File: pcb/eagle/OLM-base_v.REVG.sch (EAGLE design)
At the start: 40 parts, among them IC1 ATMEGA, IC2 MCP1702-33, IC3 ENC28J60SP, IC4 DS1307, J1 POWER_JACKPTH, J2 MAGJACK, U1 USD-SOCKETMICRO-SD-SOCKET-TAO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, X1 16 MHz, X2 25MHz, X3 32.657k

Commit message: made changes
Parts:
- removed JP1: BATT, SparkFun:M02LOCK_LONGPADS
- removed JP2: (no value), SparkFun-Connectors:M08LOCK
- added CN1: (no value), adafruit:JST_2PIN-THM-RA
- added JP4: M10LOCK, SparkFun-Connectors:M10LOCK
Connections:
- net A4/SDA: now also JP4.10; no longer JP2.8
- net A5/SCL: now also JP4.9; no longer JP2.7
- net D2: now also JP4.3; no longer JP2.4
- net D3/PWM: now also JP4.2; no longer JP2.3
- net D4: now also JP4.6
- net D6/PWM: now also JP4.5
- net D7: now also JP4.4
- net E-CLK: now also JP4.8; no longer JP2.6
- net E-INT: now also JP4.7; no longer JP2.5
- net GND: now also CN1.1, JP4.1; no longer JP1.2, JP2.1
- net MISO/D12: now also U1.DO
- net MOSI/D11: now also U1.DI
- net SCK/D13: now also U1.SCK
- net VCC: now also JP3.8; no longer JP2.2
- net VIN: now also CN1.2; no longer JP1.1, JP3.8
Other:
- note added: "328p"
- note added: "Breakout"
- note added: "Ethernet"
- note added: "RTC"
- note added: "uSD"
- note removed: "UNO-Compatible"
- moved on the sheet: BAT1, CR, IC4, JP3, RN1-2, RN1-3, RN1-4, RN1-5, U1, X3

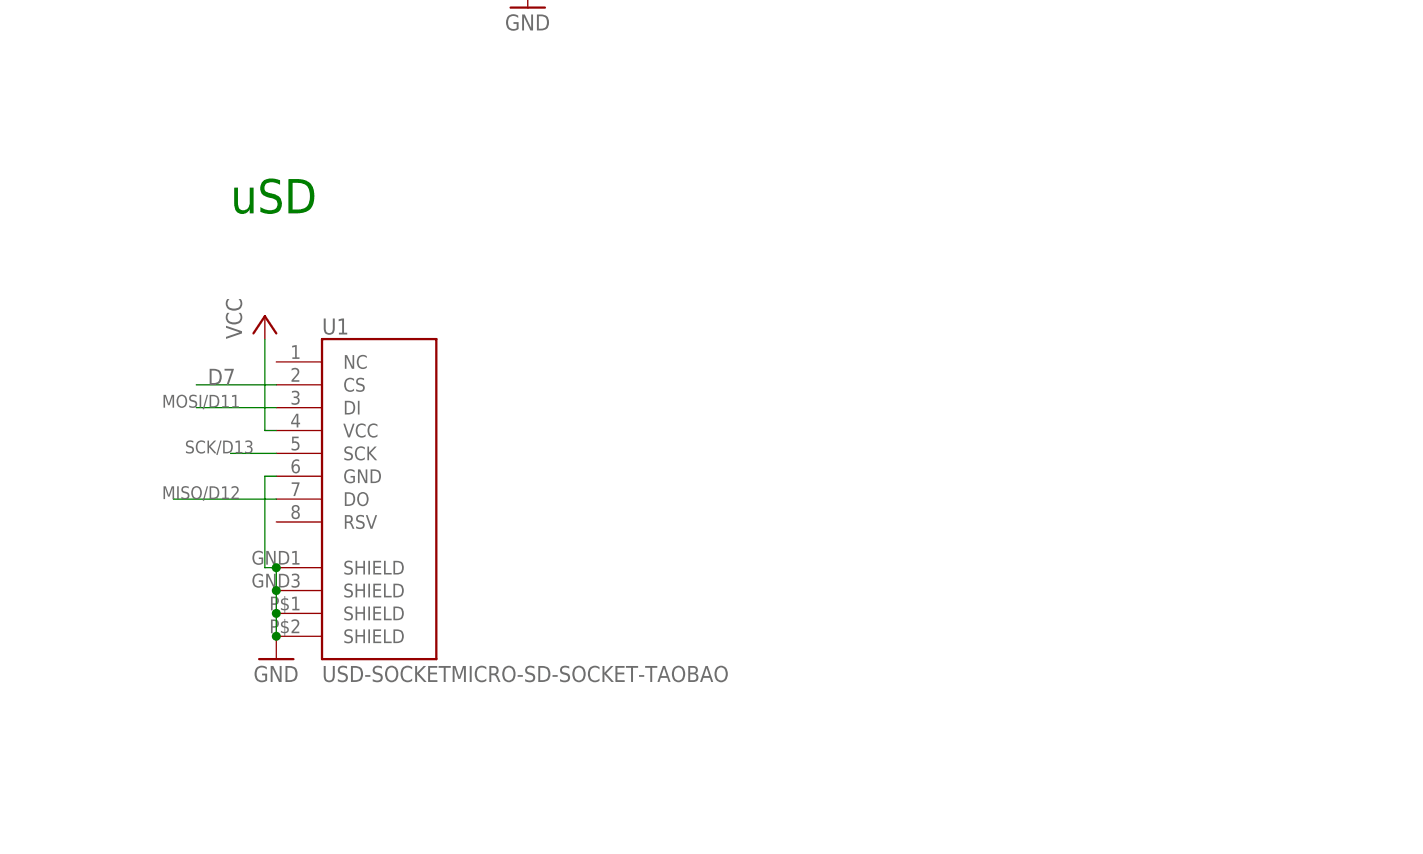
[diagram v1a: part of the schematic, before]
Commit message: rewired OLM-base-REVG
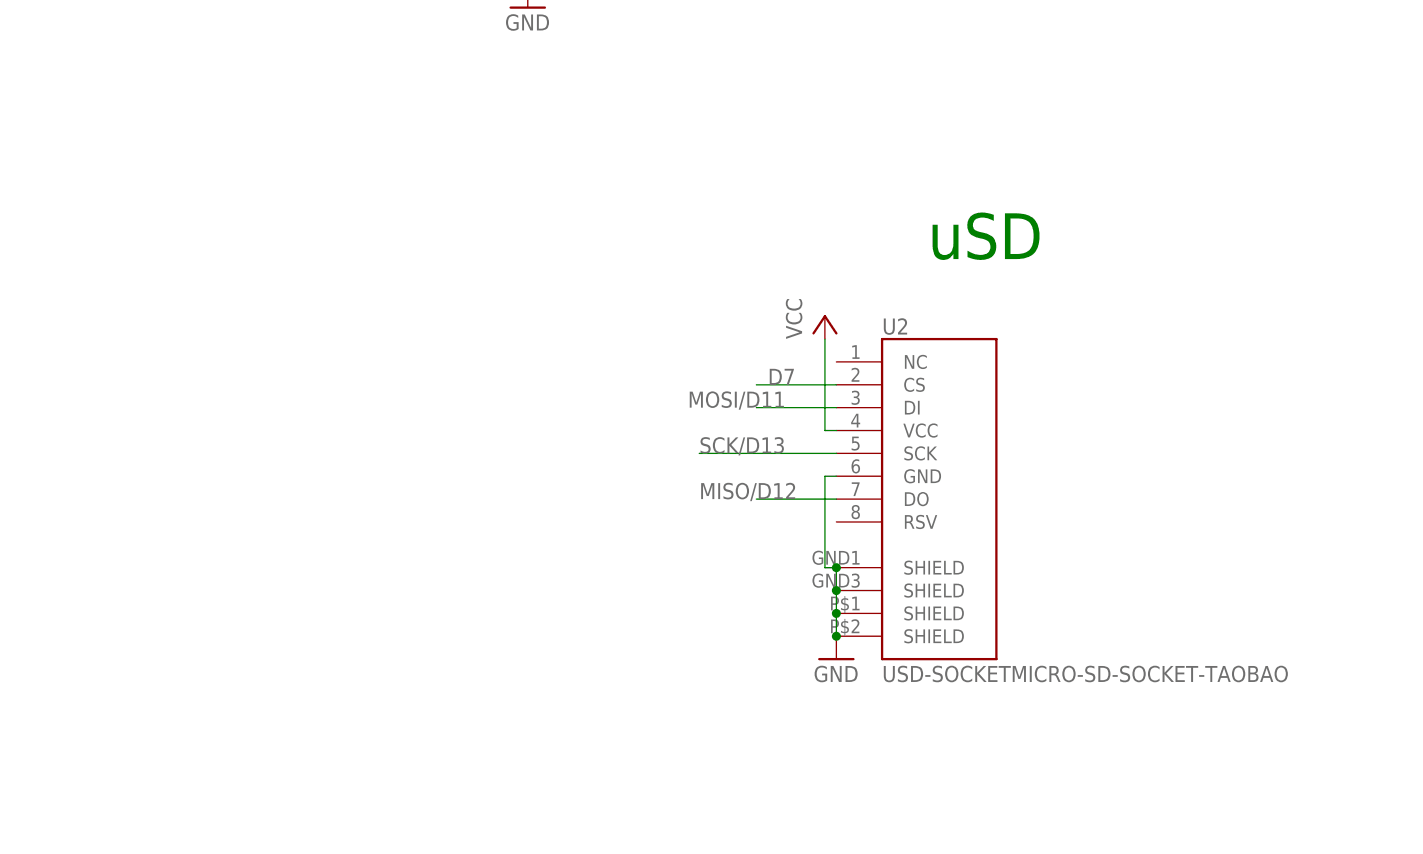
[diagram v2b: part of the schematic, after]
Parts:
- removed U1: USD-SOCKETMICRO-SD-SOCKET-TAOBAO, SparkFunNew:USD-SOCKETMICRO-SD-SOCKET-TAOBAO
- added U2: USD-SOCKETMICRO-SD-SOCKET-TAOBAO, SparkFunNew:USD-SOCKETMICRO-SD-SOCKET-TAOBAO
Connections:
- net D7: now also U2.CS; no longer U1.CS
- net GND: now also U2.GND, U2.SHIELD@1, U2.SHIELD@2, U2.SHIELD@3, U2.SHIELD@4; no longer U1.GND, U1.SHIELD@1, U1.SHIELD@2, U1.SHIELD@3, U1.SHIELD@4
- net MISO/D12: now also U2.DO; no longer U1.DO
- net MOSI/D11: now also U2.DI; no longer U1.DI
- net SCK/D13: now also U2.SCK; no longer U1.SCK
- net VCC: now also U2.VCC; no longer U1.VCC
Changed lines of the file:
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@@
 <part name="RN1" library="resistor-net" deviceset="RNX7" device=""/>
 <part name="JP3" library="SparkFun-Connectors" deviceset="M08" device="LOCK"/>
-<part name="U1" library="SparkFunNew" deviceset="USD-SOCKET" device="MICRO-SD-SOCKET-TAOBAO" value="USD-SOCKETMICRO-SD-SOCKET-TAOBAO"/>
-<part name="GND5" library="SparkFun" deviceset="GND" device=""/>
-<part name="+3V3" library="supply1" deviceset="VCC" device=""/>
 <part name="JP4" library="SparkFun-Connectors" deviceset="M10" device="LOCK"/>
 <part name="CN1" library="adafruit" deviceset="JST_2PIN" device="-THM-RA"/>
+<part name="U2" library="SparkFunNew" deviceset="USD-SOCKET" device="MICRO-SD-SOCKET-TAOBAO" value="USD-SOCKETMICRO-SD-SOCKET-TAOBAO"/>
+<part name="GND3" library="SparkFun" deviceset="GND" device=""/>
+<part name="+3V1" library="supply1" deviceset="VCC" device=""/>
 </parts>
 <sheets>
@@
 <text x="127" y="76.2" size="3.81" layer="91">Ethernet</text>
 <text x="0" y="-124.46" size="3.81" layer="91">RTC</text>
-<text x="91.44" y="-93.98" size="3.81" layer="91">uSD</text>
+<text x="168.91" y="-99.06" size="5.08" layer="91">uSD</text>
 </plain>
 <instances>
@@
 <instance part="RN1" gate="-5" x="8.89" y="-157.48" rot="MR90"/>
 <instance part="JP3" gate="G$1" x="35.56" y="-25.4"/>
-<instance part="U1" gate="G$1" x="104.14" y="-123.19"/>
-<instance part="GND5" gate="1" x="96.52" y="-143.51"/>
-<instance part="+3V3" gate="VCC" x="95.25" y="-105.41"/>
 <instance part="JP4" gate="G$1" x="-10.16" y="-17.78"/>
 <instance part="CN1" gate="G$1" x="-43.18" y="-91.44"/>
+<instance part="U2" gate="G$1" x="166.37" y="-123.19"/>
+<instance part="GND3" gate="1" x="158.75" y="-143.51"/>
+<instance part="+3V1" gate="VCC" x="157.48" y="-105.41"/>
 </instances>
 <busses>
@@
 </segment>
 <segment>
-<pinref part="U1" gate="G$1" pin="SHIELD@1"/>
-<pinref part="U1" gate="G$1" pin="SHIELD@2"/>
-<wire x1="96.52" y1="-133.35" x2="96.52" y2="-135.89" width="0.1524" layer="91"/>
-<pinref part="U1" gate="G$1" pin="SHIELD@3"/>
-<wire x1="96.52" y1="-135.89" x2="96.52" y2="-138.43" width="0.1524" layer="91"/>
-<junction x="96.52" y="-135.89"/>
-<pinref part="U1" gate="G$1" pin="SHIELD@4"/>
-<wire x1="96.52" y1="-138.43" x2="96.52" y2="-140.97" width="0.1524" layer="91"/>
-<junction x="96.52" y="-138.43"/>
-<pinref part="GND5" gate="1" pin="GND"/>
-<junction x="96.52" y="-140.97"/>
-<pinref part="U1" gate="G$1" pin="GND"/>
-<wire x1="96.52" y1="-123.19" x2="95.25" y2="-123.19" width="0.1524" layer="91"/>
-<wire x1="95.25" y1="-123.19" x2="95.25" y2="-133.35" width="0.1524" layer="91"/>
-<wire x1="95.25" y1="-133.35" x2="96.52" y2="-133.35" width="0.1524" layer="91"/>
-<junction x="96.52" y="-133.35"/>
-</segment>
-<segment>
 <pinref part="JP4" gate="G$1" pin="1"/>
 <wire x1="0" y1="-35.56" x2="7.62" y2="-35.56" width="0.1524" layer="91"/>
 <label x="7.62" y="-35.56" size="1.778" layer="95"/>
+</segment>
+<segment>
+<pinref part="U2" gate="G$1" pin="SHIELD@1"/>
+<pinref part="U2" gate="G$1" pin="SHIELD@2"/>
+<wire x1="158.75" y1="-133.35" x2="158.75" y2="-135.89" width="0.1524" layer="91"/>
+<pinref part="U2" gate="G$1" pin="SHIELD@3"/>
+<wire x1="158.75" y1="-135.89" x2="158.75" y2="-138.43" width="0.1524" layer="91"/>
+<junction x="158.75" y="-135.89"/>
+<pinref part="U2" gate="G$1" pin="SHIELD@4"/>
+<wire x1="158.75" y1="-138.43" x2="158.75" y2="-140.97" width="0.1524" layer="91"/>
+<junction x="158.75" y="-138.43"/>
+<pinref part="GND3" gate="1" pin="GND"/>
+<junction x="158.75" y="-140.97"/>
+<pinref part="U2" gate="G$1" pin="GND"/>
+<wire x1="158.75" y1="-123.19" x2="157.48" y2="-123.19" width="0.1524" layer="91"/>
+<wire x1="157.48" y1="-123.19" x2="157.48" y2="-133.35" width="0.1524" layer="91"/>
+<wire x1="157.48" y1="-133.35" x2="158.75" y2="-133.35" width="0.1524" layer="91"/>
+<junction x="158.75" y="-133.35"/>
 </segment>
 </net>
@@
 </segment>
 <segment>
-<pinref part="U1" gate="G$1" pin="VCC"/>
-<wire x1="96.52" y1="-118.11" x2="95.25" y2="-118.11" width="0.1524" layer="91"/>
-<wire x1="95.25" y1="-118.11" x2="95.25" y2="-107.95" width="0.1524" layer="91"/>
-<pinref part="+3V3" gate="VCC" pin="VCC"/>
-</segment>
-<segment>
 <pinref part="JP3" gate="G$1" pin="8"/>
 <wire x1="40.64" y1="-15.24" x2="45.72" y2="-15.24" width="0.1524" layer="91"/>
 <label x="45.72" y="-15.24" size="1.778" layer="95"/>
 </segment>
+<segment>
+<pinref part="U2" gate="G$1" pin="VCC"/>
+<wire x1="158.75" y1="-118.11" x2="157.48" y2="-118.11" width="0.1524" layer="91"/>
+<wire x1="157.48" y1="-118.11" x2="157.48" y2="-107.95" width="0.1524" layer="91"/>
+<pinref part="+3V1" gate="VCC" pin="VCC"/>
+</segment>
 </net>
 <net name="A1" class="0">
@@
 </segment>
 <segment>
-<wire x1="91.44" y1="-120.65" x2="96.52" y2="-120.65" width="0.1524" layer="91"/>
-<label x="86.36" y="-120.65" size="1.4224" layer="95"/>
-<pinref part="U1" gate="G$1" pin="SCK"/>
+<pinref part="U2" gate="G$1" pin="SCK"/>
+<wire x1="158.75" y1="-120.65" x2="143.51" y2="-120.65" width="0.1524" layer="91"/>
+<label x="143.51" y="-120.65" size="1.778" layer="95"/>
 </segment>
 </net>
@@
 </segment>
 <segment>
-<wire x1="85.09" y1="-125.73" x2="96.52" y2="-125.73" width="0.1524" layer="91"/>
-<label x="83.82" y="-125.73" size="1.4224" layer="95"/>
-<pinref part="U1" gate="G$1" pin="DO"/>
+<pinref part="U2" gate="G$1" pin="DO"/>
+<wire x1="158.75" y1="-125.73" x2="149.86" y2="-125.73" width="0.1524" layer="91"/>
+<label x="143.51" y="-125.73" size="1.778" layer="95"/>
 </segment>
 </net>
@@
 </segment>
 <segment>
-<wire x1="87.63" y1="-115.57" x2="96.52" y2="-115.57" width="0.1524" layer="91"/>
-<label x="83.82" y="-115.57" size="1.4224" layer="95"/>
-<pinref part="U1" gate="G$1" pin="DI"/>
+<pinref part="U2" gate="G$1" pin="DI"/>
+<wire x1="158.75" y1="-115.57" x2="149.86" y2="-115.57" width="0.1524" layer="91"/>
+<label x="142.24" y="-115.57" size="1.778" layer="95"/>
 </segment>
 </net>
@@
 </segment>
 <segment>
-<pinref part="U1" gate="G$1" pin="CS"/>
-<wire x1="96.52" y1="-113.03" x2="87.63" y2="-113.03" width="0.1524" layer="91"/>
-<label x="88.9" y="-113.03" size="1.778" layer="95"/>
-</segment>
-<segment>
 <pinref part="JP4" gate="G$1" pin="4"/>
 <wire x1="0" y1="-27.94" x2="7.62" y2="-27.94" width="0.1524" layer="91"/>
 <label x="7.62" y="-27.94" size="1.778" layer="95"/>
 </segment>
-</net>
+<segment>
+<pinref part="U2" gate="G$1" pin="CS"/>
+<wire x1="158.75" y1="-113.03" x2="149.86" y2="-113.03" width="0.1524" layer="91"/>
+<label x="151.13" y="-113.03" size="1.778" layer="95"/>
+</segment>
+</net>

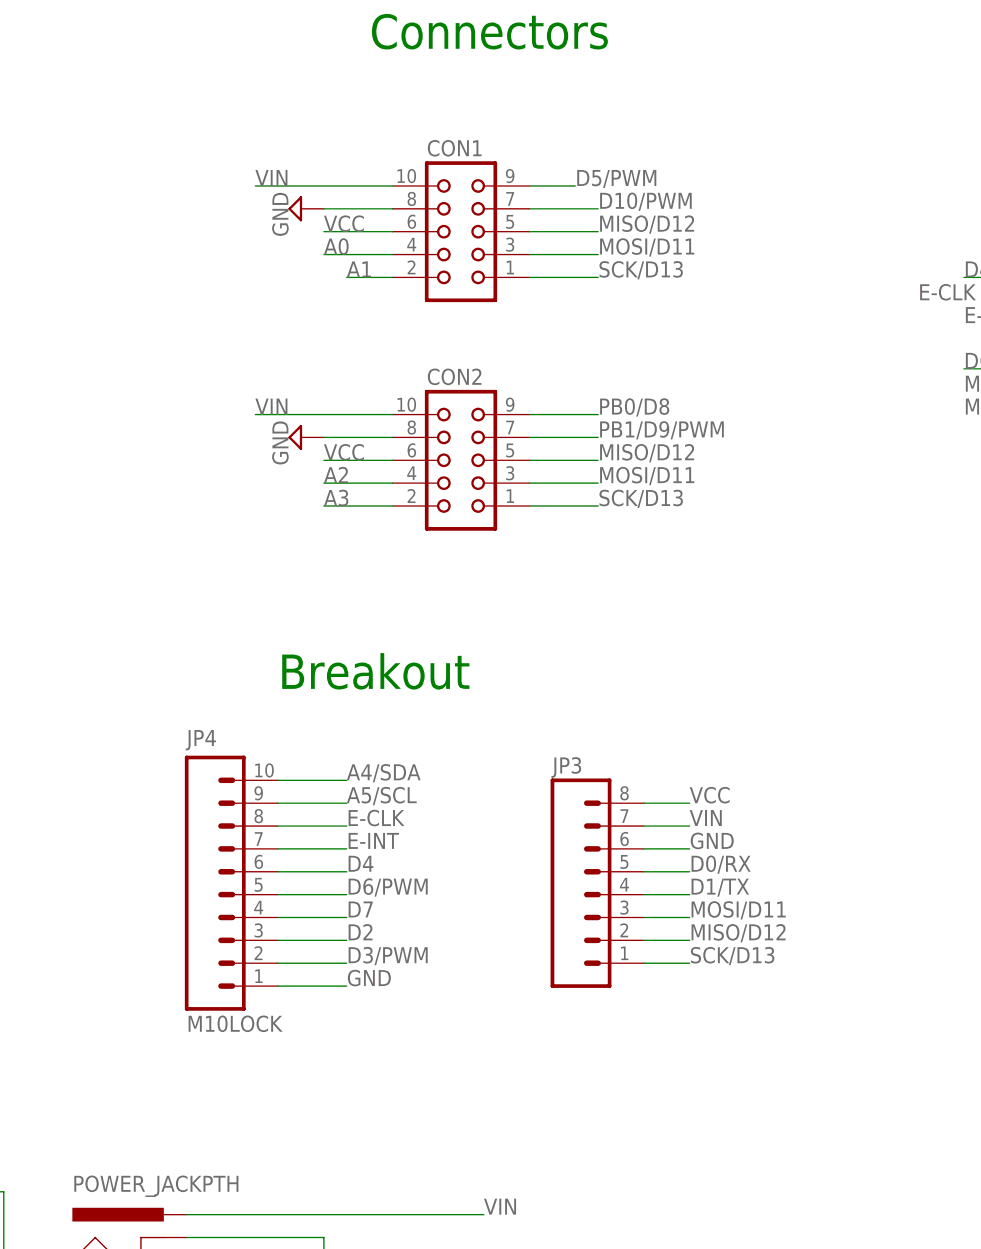
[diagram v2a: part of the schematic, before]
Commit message: fixed breakouts by adding reset pin
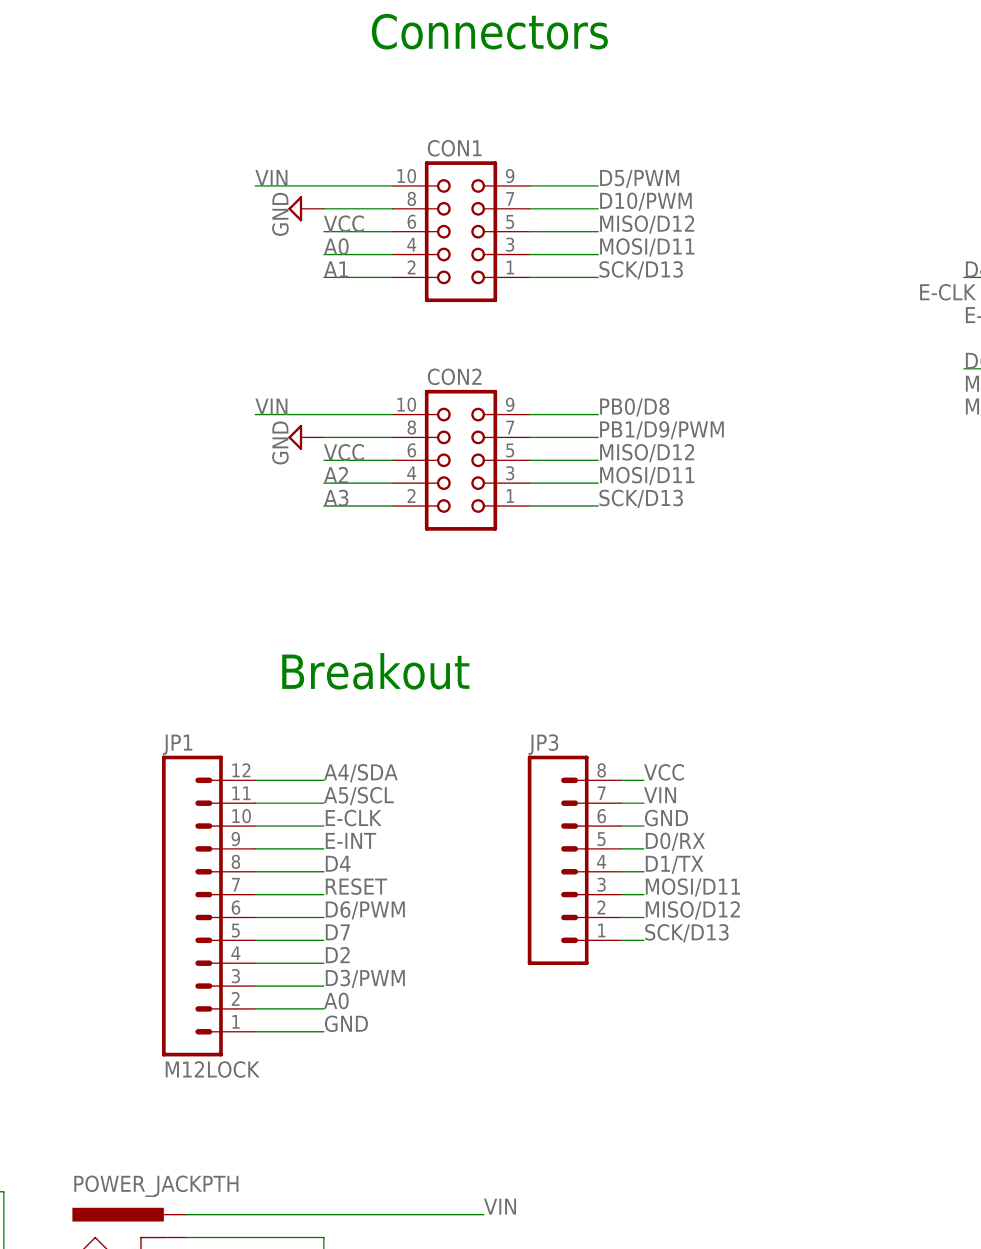
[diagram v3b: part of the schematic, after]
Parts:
- removed JP4: M10LOCK, SparkFun-Connectors:M10LOCK
- added JP1: M12LOCK, SparkFun-Connectors:M12LOCK
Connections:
- net A0: now also JP1.2
- net A1: now also CON1.2
- net A2: now also CON2.4
- net A3: now also CON2.2
- net A4/SDA: now also JP1.12; no longer JP4.10
- net A5/SCL: now also JP1.11; no longer JP4.9
- net D10/PWM: now also CON1.7
- net D2: now also JP1.4; no longer JP4.3
- net D3/PWM: now also JP1.3; no longer JP4.2
- net D4: now also JP1.8; no longer JP4.6
- net D5/PWM: now also CON1.9
- net D6/PWM: now also JP1.6; no longer JP4.5
- net D7: now also JP1.5; no longer JP4.4
- net E-CLK: now also JP1.10; no longer JP4.8
- net E-INT: now also JP1.9; no longer JP4.7
- net GND: now also JP1.1; no longer JP4.1
- net PB0/D8: now also CON2.9
- net PB1/D9/PWM: now also CON2.7
- net RESET: now also JP1.7
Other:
- moved on the sheet: JP3
